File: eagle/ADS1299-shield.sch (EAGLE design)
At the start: 132 parts, among them IC1 ADS1299IPAG, IC2 TPS72325DBVT, IC3 TPS73225DBVT, IC5 24AA256UID, IC6 TPS604XXDBV, IC7 OPA376DBV, IC8 OPA376DBV, IC9 TXS0102DCTR, J8 Electrode Connector, U2 TXB0108PWR, U3 TXB0108PWR

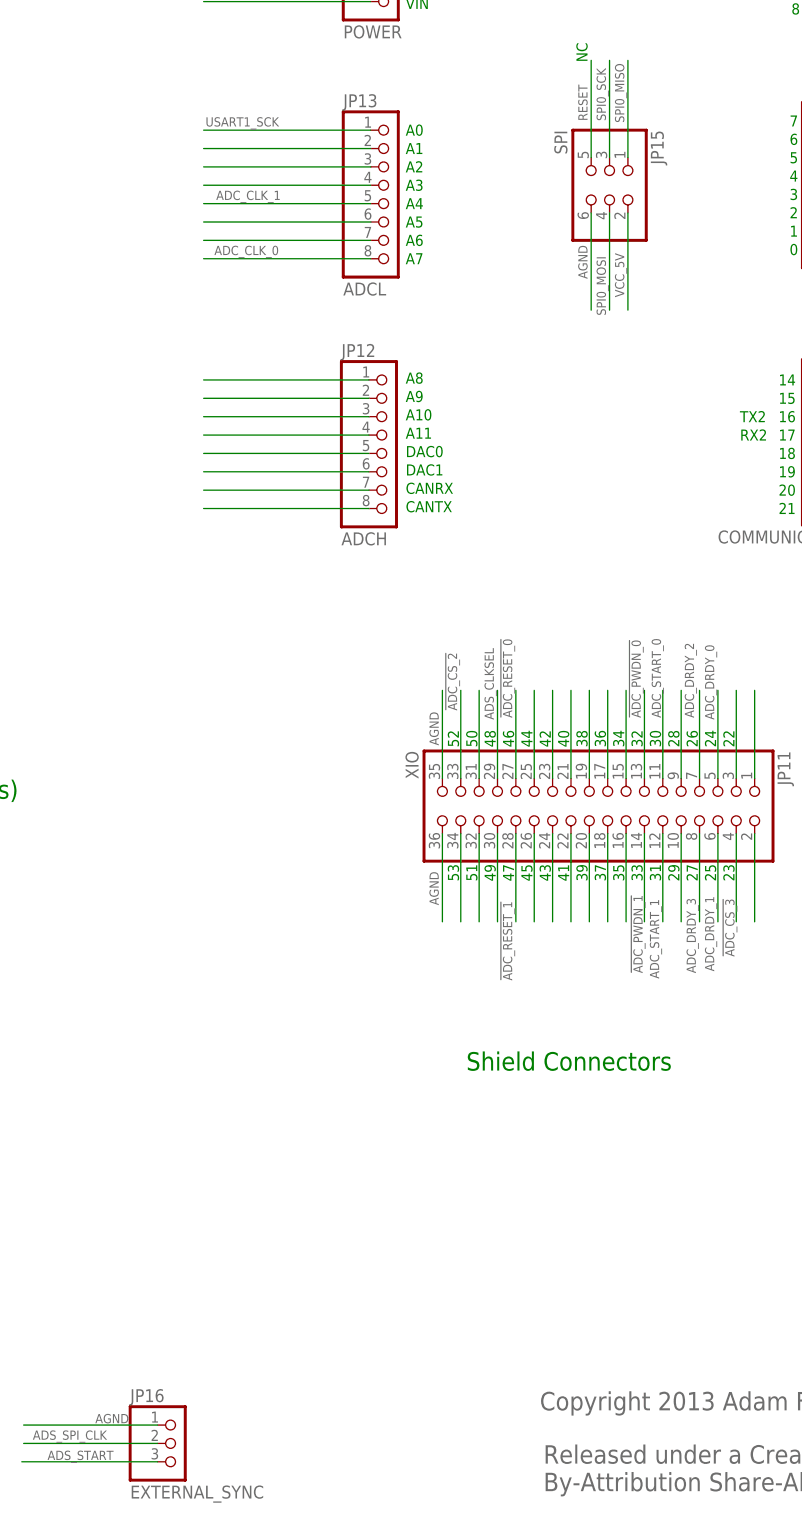
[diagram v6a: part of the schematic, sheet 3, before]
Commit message: updated headers in SmartPrj to have smaller pads; moved traces away from edge of board; minor clearance improvements; documentation labels for configuration jumpers partly done
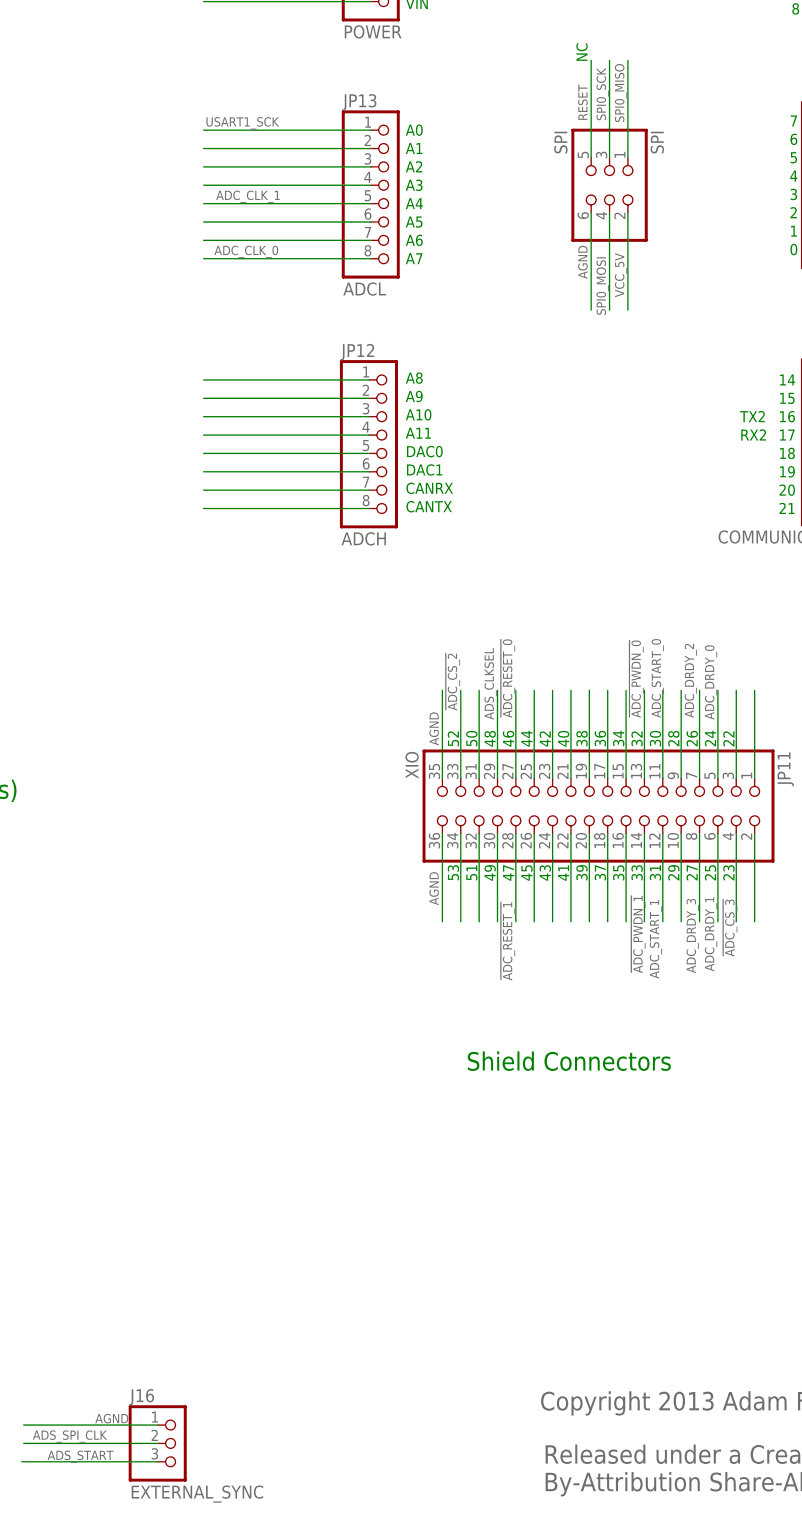
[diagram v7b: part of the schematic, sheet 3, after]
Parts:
- renumbered JP15 to SPI, JP16 to J16
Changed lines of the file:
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@@
 <part name="JP8" library="SmartPrj" deviceset="PINHD-1X10" device="" value="PWMH"/>
 <part name="JP14" library="SmartPrj" deviceset="PINHD-1X8" device="" value="POWER"/>
-<part name="JP15" library="SmartPrj" deviceset="PINHD-2X3" device="" value="SPI"/>
+<part name="SPI" library="SmartPrj" deviceset="PINHD-2X3" device="" value="SPI"/>
 <part name="TP1" library="adafruit" deviceset="PINHD-1X1" device="" value="AVDD_TEST_POINT"/>
 <part name="TP2" library="adafruit" deviceset="PINHD-1X1" device="" value="AVSS_TEST_POINT"/>
@@
 <part name="R34" library="SparkFun-Passives" deviceset="RESISTOR" device="0603-RES" value="4.99k"/>
 <part name="SUPPLY51" library="supply2" deviceset="AGND" device=""/>
-<part name="JP16" library="adafruit" deviceset="JST_3PIN" device="" value="EXTERNAL_SYNC"/>
+<part name="J16" library="adafruit" deviceset="JST_3PIN" device="" value="EXTERNAL_SYNC"/>
 <part name="JP2" library="headers" deviceset="PINHD-2X10" device="" value="CONFIG3"/>
 <part name="R2" library="SparkFun-Passives" deviceset="RESISTOR" device="0603-RES" value="10k"/>
@@
 <instance part="JP8" gate="A" x="363.982" y="244.348" rot="MR0"/>
 <instance part="JP14" gate="A" x="304.8" y="240.03"/>
-<instance part="JP15" gate="A" x="335.28" y="208.28" rot="R270"/>
+<instance part="SPI" gate="A" x="335.28" y="208.28" rot="R270"/>
 <instance part="U$5" gate="G$1" x="226.06" y="134.62"/>
 <instance part="U$6" gate="G$1" x="236.22" y="134.62"/>
@@
 <attribute name="VALUE" x="16.383" y="180.721" size="1.778" layer="96" rot="R180"/>
 </instance>
-<instance part="JP16" gate="G$1" x="275.336" y="33.02"/>
+<instance part="J16" gate="G$1" x="275.336" y="33.02"/>
 <instance part="JP2" gate="A" x="198.12" y="40.894"/>
 <instance part="R2" gate="G$1" x="25.908" y="226.822" smashed="yes">
@@
 </segment>
 <segment>
-<pinref part="JP15" gate="A" pin="6"/>
+<pinref part="SPI" gate="A" pin="6"/>
 <wire x1="332.74" y1="203.2" x2="332.74" y2="189.738" width="0.1524" layer="91"/>
 <label x="332.232" y="194.056" size="1.27" layer="95" rot="R90"/>
@@
 <wire x1="272.796" y1="35.56" x2="254.254" y2="35.56" width="0.1524" layer="91"/>
 <label x="264.16" y="35.814" size="1.27" layer="95"/>
-<pinref part="JP16" gate="G$1" pin="1"/>
+<pinref part="J16" gate="G$1" pin="1"/>
 </segment>
 </net>
@@
 <wire x1="272.796" y1="33.02" x2="254.254" y2="33.02" width="0.1524" layer="91"/>
 <label x="255.524" y="33.528" size="1.27" layer="95"/>
-<pinref part="JP16" gate="G$1" pin="2"/>
+<pinref part="J16" gate="G$1" pin="2"/>
 </segment>
 <segment>
@@
 </segment>
 <segment>
-<pinref part="JP16" gate="G$1" pin="3"/>
+<pinref part="J16" gate="G$1" pin="3"/>
 <wire x1="272.796" y1="30.48" x2="254" y2="30.48" width="0.1524" layer="91"/>
 <label x="257.556" y="30.734" size="1.27" layer="95"/>
@@
 <net name="SPI0_MOSI" class="0">
 <segment>
-<pinref part="JP15" gate="A" pin="4"/>
+<pinref part="SPI" gate="A" pin="4"/>
 <wire x1="335.28" y1="203.2" x2="335.28" y2="189.738" width="0.1524" layer="91"/>
 <label x="334.772" y="188.976" size="1.27" layer="95" rot="R90"/>
@@
 </segment>
 <segment>
-<pinref part="JP15" gate="A" pin="1"/>
+<pinref part="SPI" gate="A" pin="1"/>
 <wire x1="337.82" y1="210.82" x2="337.82" y2="224.282" width="0.1524" layer="91"/>
 <label x="337.312" y="215.646" size="1.27" layer="95" rot="R90"/>
@@
 <net name="VCC_5V" class="0">
 <segment>
-<pinref part="JP15" gate="A" pin="2"/>
+<pinref part="SPI" gate="A" pin="2"/>
 <wire x1="337.82" y1="203.2" x2="337.82" y2="189.738" width="0.1524" layer="91"/>
 <label x="337.312" y="191.516" size="1.27" layer="95" rot="R90"/>
@@
 <net name="RESET" class="0">
 <segment>
-<pinref part="JP15" gate="A" pin="5"/>
+<pinref part="SPI" gate="A" pin="5"/>
 <wire x1="332.74" y1="210.82" x2="332.74" y2="224.282" width="0.1524" layer="91"/>
 <label x="332.232" y="215.9" size="1.27" layer="95" rot="R90"/>
@@
 <net name="SPI0_SCK" class="0">
 <segment>
-<pinref part="JP15" gate="A" pin="3"/>
+<pinref part="SPI" gate="A" pin="3"/>
 <wire x1="335.28" y1="210.82" x2="335.28" y2="224.282" width="0.1524" layer="91"/>
 <label x="334.772" y="215.9" size="1.27" layer="95" rot="R90"/>

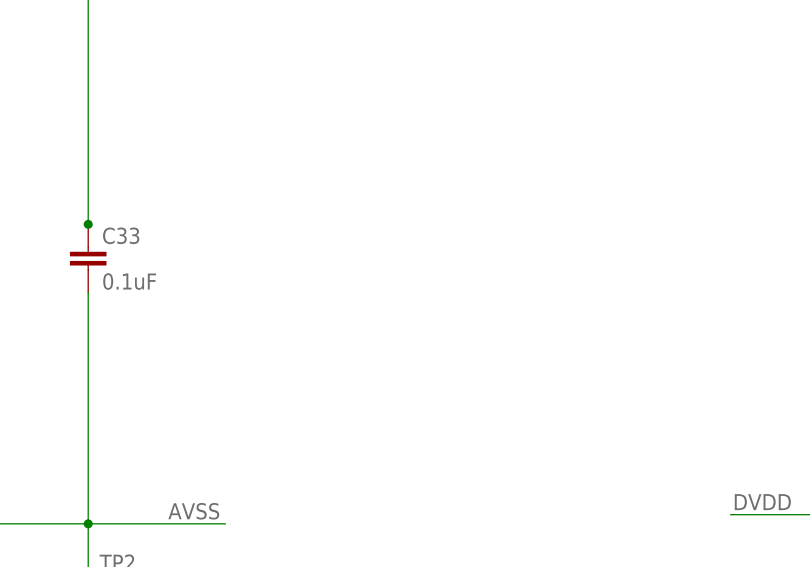
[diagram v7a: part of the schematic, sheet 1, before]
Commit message: documentation labels done; OSH and CC logos on back of board; increased size of component names for better readability
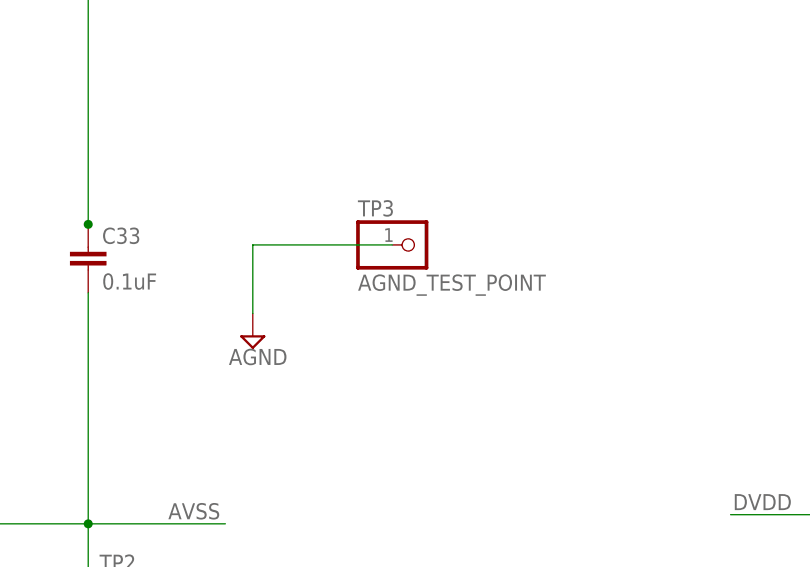
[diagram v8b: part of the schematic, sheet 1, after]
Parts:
- added TP3: AGND_TEST_POINT, adafruit:PINHD-1X1
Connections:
- net AGND: now also TP3.1
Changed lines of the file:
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@@
 <part name="SUPPLY54" library="supply2" deviceset="AGND" device=""/>
 <part name="R4" library="SparkFun-Passives" deviceset="RESISTOR" device="0603-RES" value="10k"/>
+<part name="TP3" library="adafruit" deviceset="PINHD-1X1" device="" value="AGND_TEST_POINT"/>
+<part name="SUPPLY55" library="supply2" deviceset="AGND" device=""/>
 </parts>
 <sheets>
@@
 <instance part="TP1" gate="G$1" x="184.912" y="113.792"/>
 <instance part="TP2" gate="G$1" x="184.15" y="33.782"/>
+<instance part="TP3" gate="G$1" x="212.852" y="73.152"/>
+<instance part="SUPPLY55" gate="G$1" x="194.818" y="62.992"/>
 </instances>
 <busses>
@@
 <wire x1="283.972" y1="43.18" x2="283.972" y2="39.37" width="0.1524" layer="91"/>
 </segment>
-</net>
+<segment>
+<pinref part="TP3" gate="G$1" pin="1"/>
+<wire x1="210.312" y1="73.152" x2="194.818" y2="73.152" width="0.1524" layer="91"/>
+<wire x1="194.818" y1="73.152" x2="194.818" y2="65.532" width="0.1524" layer="91"/>
+<pinref part="SUPPLY55" gate="G$1" pin="AGND"/>
+</segment>
+</net>
